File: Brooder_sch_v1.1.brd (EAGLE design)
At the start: 90 x 75 mm, 38 parts, among them J1 DCJ0202, J2 1X2-3.5MM, J3 DCJ0202, J4 1X2-3.5MM, T1 2N2222, U1 328P

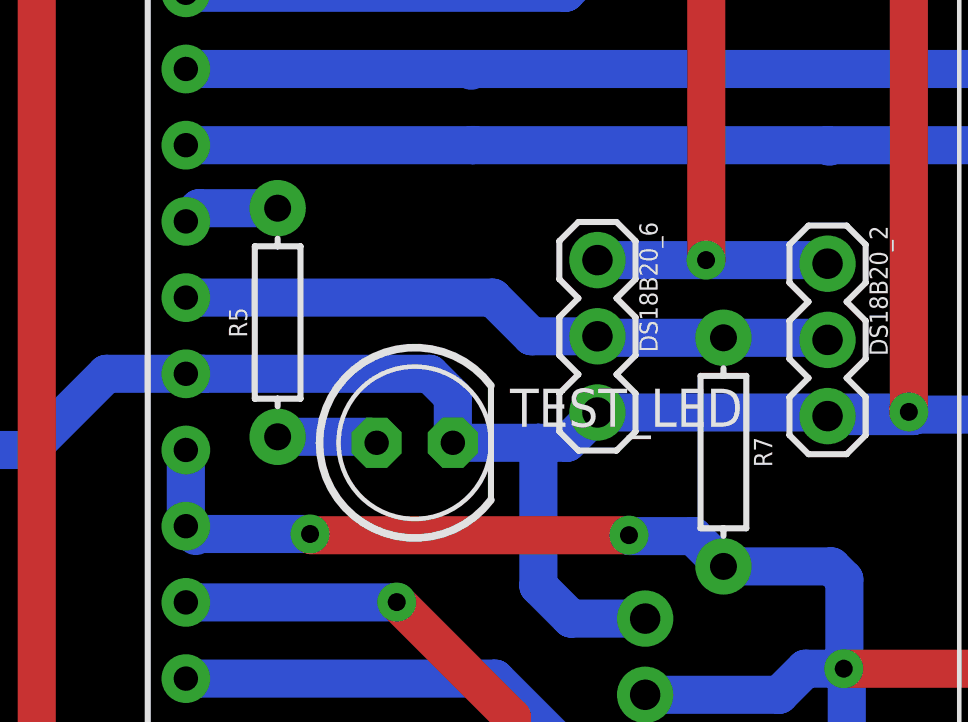
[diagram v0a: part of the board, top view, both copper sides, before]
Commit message: Removes test led fro  schematic
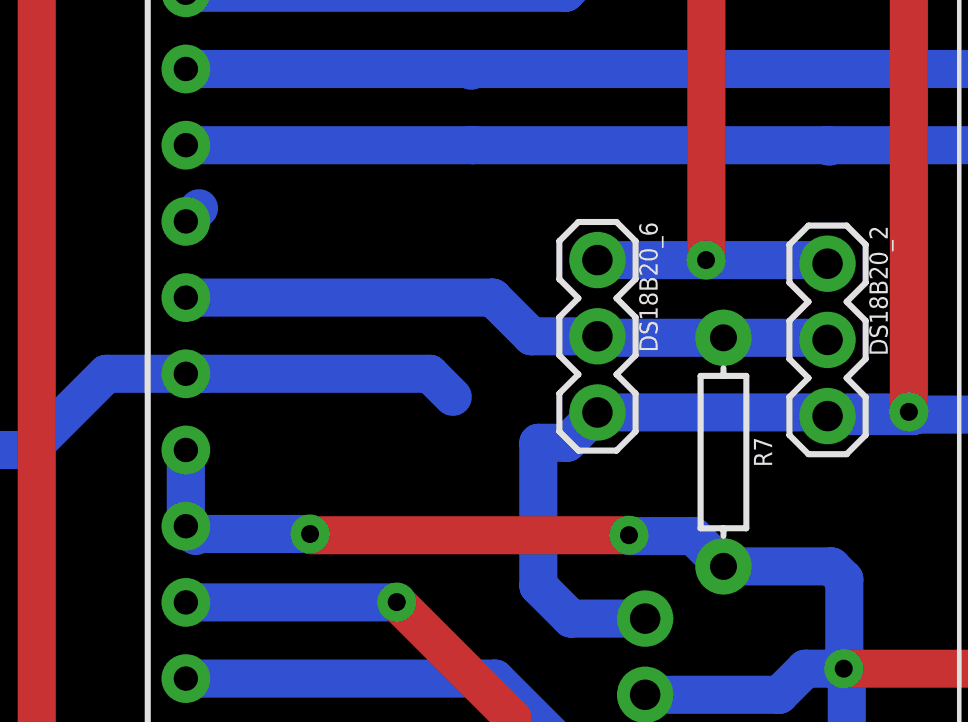
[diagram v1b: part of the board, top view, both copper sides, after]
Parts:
- removed R5: 220, SparkFun-Resistors:AXIAL-0.3
- removed TEST_LED: (no value), adafruit:LED5MM
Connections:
- removed net N$1: R5.P$1, TEST_LED.A
- net GND: no longer TEST_LED.K
- net PC1: no longer R5.P$2
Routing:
- net GND: track 386.0 -> 381.6 mm
- net N$1: track 3.38 -> 0.00 mm
- net PC1: track 3.24 -> 0.62 mm
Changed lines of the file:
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@@
 </element>
 <element name="J2" library="adafruit" package="1X2-3.5MM" value="1X2-3.5MM" x="69.84" y="69.63"/>
-<element name="R5" library="SparkFun-Resistors" package="AXIAL-0.3" value="220" x="45" y="43" rot="R90">
-<attribute name="PROD_ID" value="RES-09327" x="45" y="43" size="1.778" layer="27" rot="R90" display="off"/>
-</element>
-<element name="TEST_LED" library="adafruit" package="LED5MM" value="" x="49.57" y="38.99"/>
 <element name="DS3231" library="SparkFun-Connectors" package="1X06_NO_SILK" value="" x="49.13" y="61.27">
 <attribute name="PROD_ID" value="CONN-08437" x="49.13" y="61.27" size="1.778" layer="27" display="off"/>
@@
 <wire x1="20.24" y1="41.49" x2="19.72" y2="40.97" width="1.27" layer="16"/>
 <contactref element="FTDI" pad="2"/>
-<contactref element="TEST_LED" pad="K"/>
 <contactref element="DS3231" pad="6"/>
 <wire x1="4.31" y1="63.03" x2="14.31" y2="63.03" width="1.27" layer="1"/>
@@
 <wire x1="3.8" y1="24.42" x2="3.05" y2="24.42" width="1.27" layer="1"/>
 <wire x1="41.94" y1="41.29" x2="50.07" y2="41.29" width="1.27" layer="16"/>
-<wire x1="50.84" y1="40.52" x2="50.84" y2="38.99" width="1.27" layer="16"/>
 <wire x1="50.07" y1="41.29" x2="50.84" y2="40.52" width="1.27" layer="16"/>
-<wire x1="50.84" y1="38.99" x2="53.69" y2="38.99" width="1.27" layer="16"/>
 <wire x1="53.69" y1="38.99" x2="54.65" y2="38.99" width="1.27" layer="16"/>
 <wire x1="54.65" y1="38.99" x2="55.66" y2="40" width="1.27" layer="16"/>
@@
 <wire x1="5" y1="7" x2="4.19" y2="14.85" width="0" layer="19" extent="16-16"/>
 <wire x1="20.24" y1="41.49" x2="13.87" y2="52.87" width="0" layer="19" extent="1-16"/>
+<wire x1="53.69" y1="38.99" x2="50.84" y2="40.52" width="0" layer="19" extent="16-16"/>
 <wire x1="19.71" y1="34.8" x2="19.72" y2="39.62" width="0" layer="19" extent="1-1"/>
 <wire x1="1.4" y1="-82.36" x2="13" y2="2" width="0" layer="19" extent="16-16"/>
@@
 <wire x1="33.25" y1="5.25" x2="33.46" y2="5.46" width="1.27" layer="16"/>
 </signal>
-<signal name="N$1">
-<contactref element="R5" pad="P$1"/>
-<contactref element="TEST_LED" pad="A"/>
-<wire x1="45" y1="39.19" x2="48.1" y2="39.19" width="1.27" layer="16"/>
-<wire x1="48.1" y1="39.19" x2="48.3" y2="38.99" width="1.27" layer="16"/>
-</signal>
 <signal name="PC1">
 <contactref element="U1" pad="24"/>
-<contactref element="R5" pad="P$2"/>
 <wire x1="41.94" y1="46.37" x2="42.38" y2="46.81" width="1.27" layer="16"/>
-<wire x1="42.38" y1="46.81" x2="45" y2="46.81" width="1.27" layer="16"/>
 <contactref element="R6" pad="P$2"/>
 <wire x1="11.81" y1="-66.35" x2="41.94" y2="46.37" width="0" layer="19" extent="1-1"/>

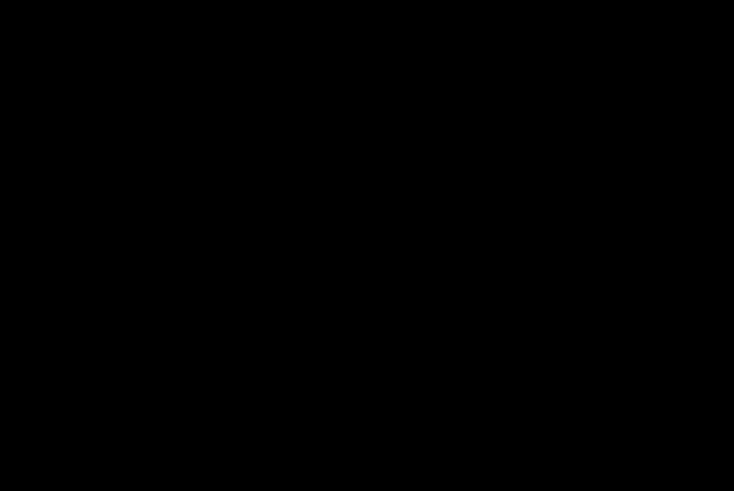
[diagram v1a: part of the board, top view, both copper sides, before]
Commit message: Adds extra terminal block to the relay
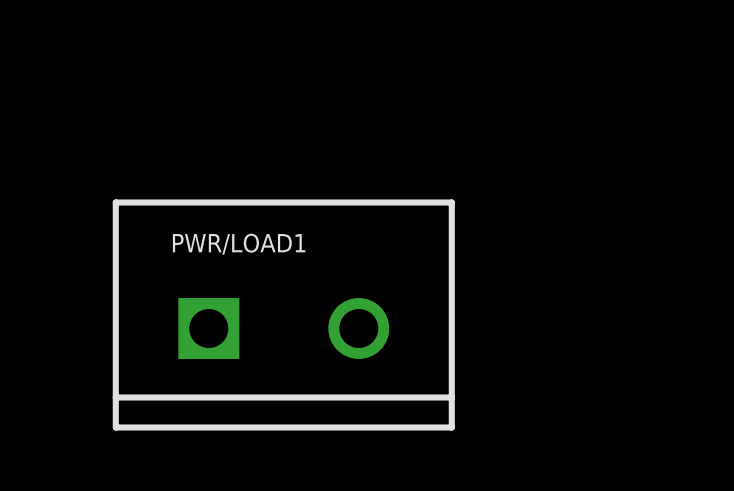
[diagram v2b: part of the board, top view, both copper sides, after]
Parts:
- added PWR/LOAD1: (no value), SparkFun-Connectors:SCREWTERMINAL-5MM-2
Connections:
- removed net N$14: PWR/LOAD.2, U$1.SWCOMMON
- new net N$1: PWR/LOAD1.2, U$1.SWCOMMON
- new net N$3: PWR/LOAD.2, PWR/LOAD1.1
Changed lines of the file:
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@@
 </element>
 <element name="LED2" library="adafruit" package="LED5MM" value="" x="30.86" y="-65.34"/>
+<element name="PWR/LOAD1" library="SparkFun-Connectors" package="SCREWTERMINAL-5MM-2" value="" x="4.96" y="-99.13">
+<attribute name="SF_SKU" value="PRT-08432" x="4.96" y="-99.13" size="1.778" layer="27" display="off"/>
+</element>
 </elements>
 <signals>
@@
 <wire x1="33.04" y1="-21.72" x2="15.84" y2="-30.6" width="0" layer="19" extent="1-1"/>
 </signal>
-<signal name="N$14">
+<signal name="N$1">
+<contactref element="PWR/LOAD1" pad="2"/>
 <contactref element="U$1" pad="SWCOMMON"/>
+<wire x1="1.84" y1="-24.6" x2="9.96" y2="-99.13" width="0" layer="19" extent="1-1"/>
+</signal>
+<signal name="N$3">
 <contactref element="PWR/LOAD" pad="2"/>
-<wire x1="38.04" y1="-21.72" x2="1.84" y2="-24.6" width="0" layer="19" extent="1-1"/>
+<contactref element="PWR/LOAD1" pad="1"/>
+<wire x1="38.04" y1="-21.72" x2="4.96" y2="-99.13" width="0" layer="19" extent="1-1"/>
 </signal>
 </signals>

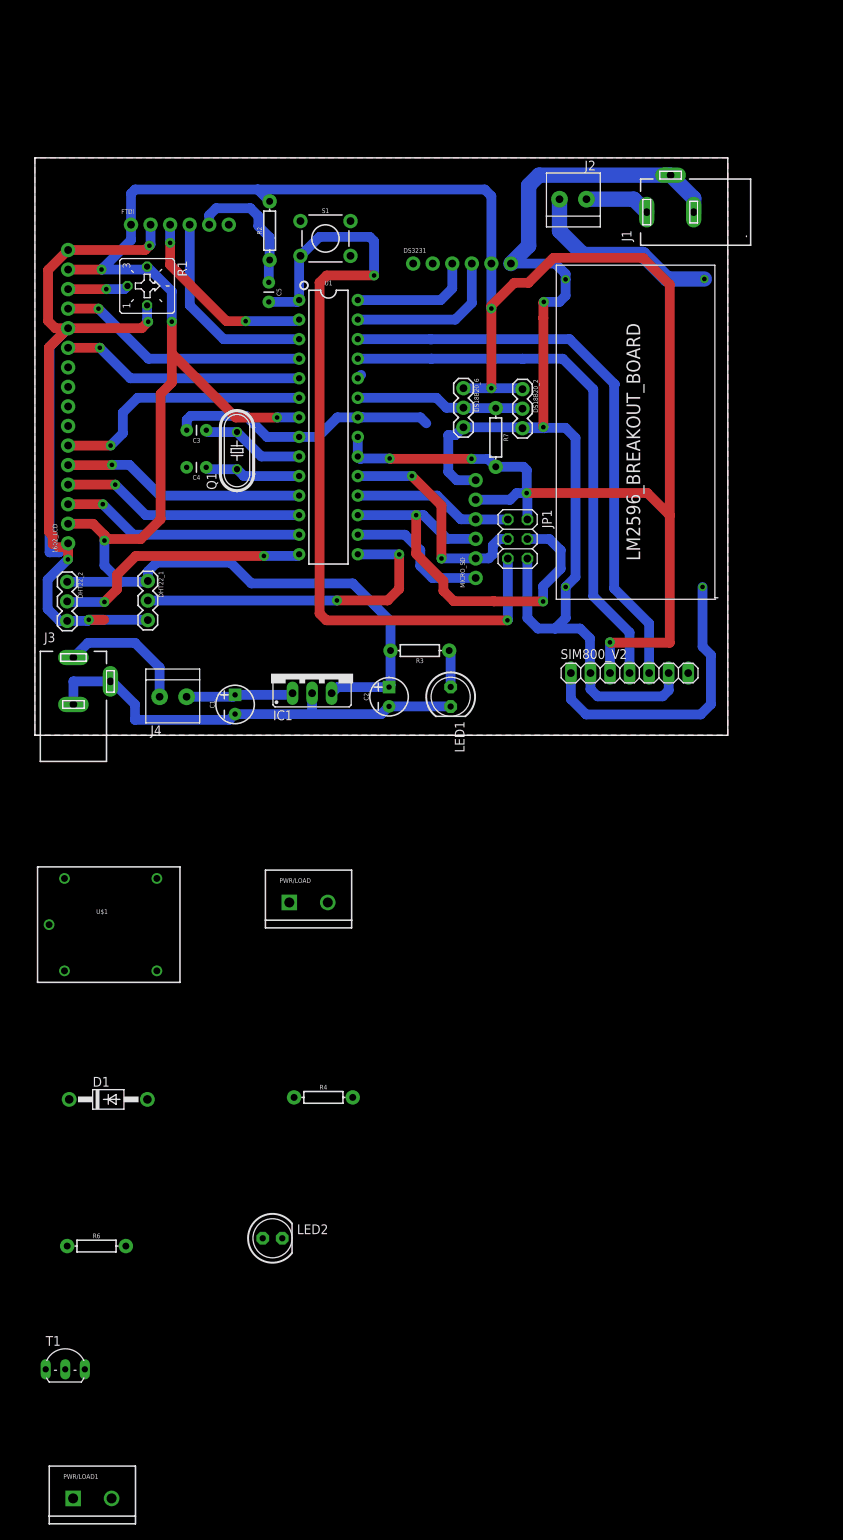
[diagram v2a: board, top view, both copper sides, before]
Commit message: Increases the size of the board from 90*75mm to 100*90mm
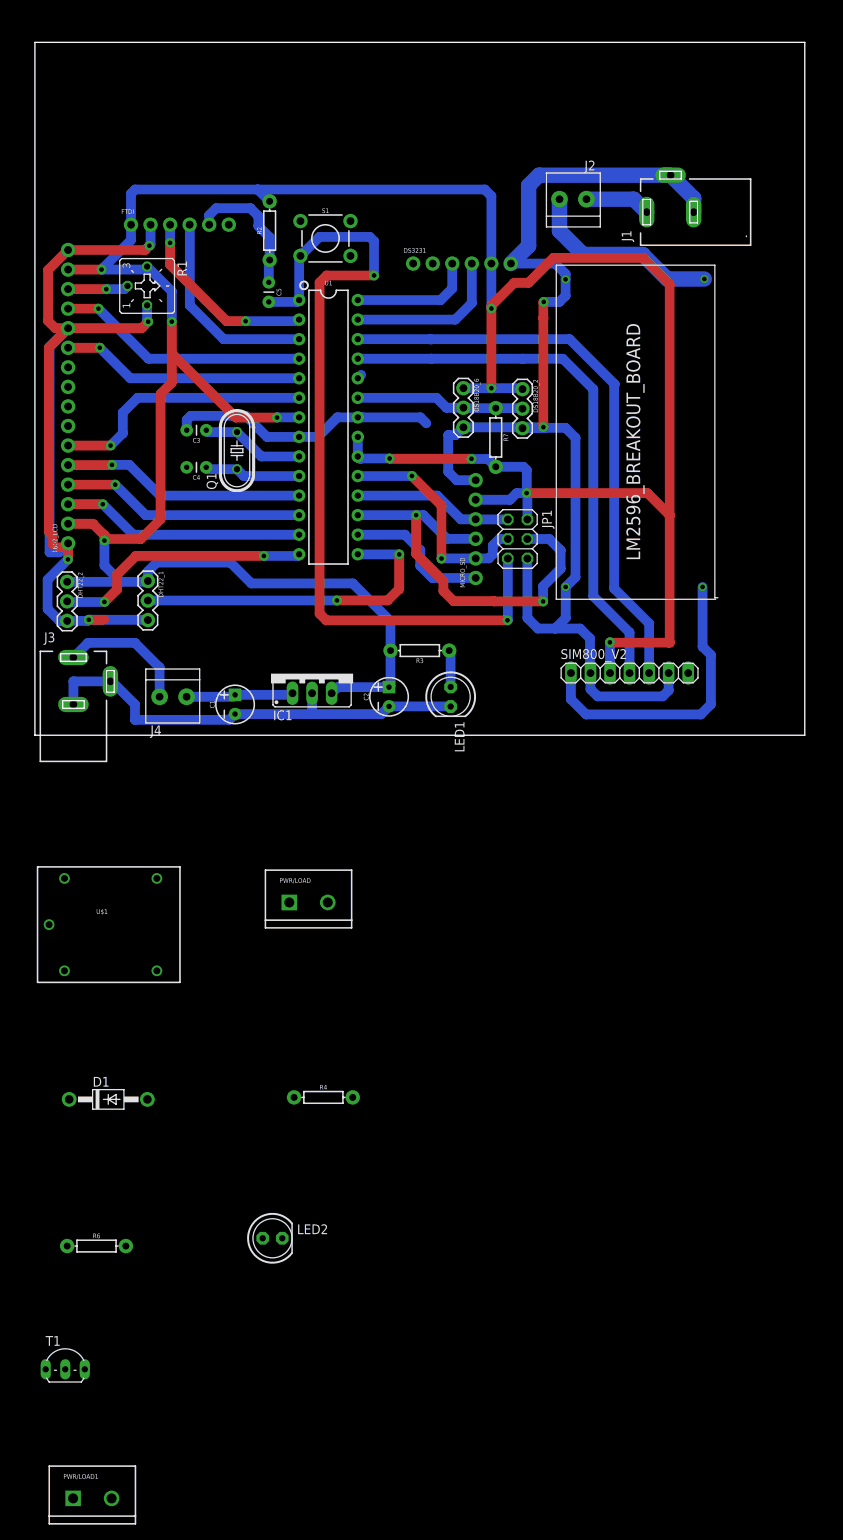
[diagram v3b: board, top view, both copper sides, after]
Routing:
- removed copper zone on layer 1, net GND
- removed copper zone on layer 16, net GND
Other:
- board size 90 x 75 mm -> 100 x 90 mm
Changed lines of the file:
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@@
 <setting verticaltext="up"/>
 </settings>
-<grid distance="0.01" unitdist="mm" unit="mm" style="lines" multiple="1" display="no" altdistance="5" altunitdist="mil" altunit="mil"/>
+<grid distance="1" unitdist="mm" unit="mm" style="lines" multiple="1" display="yes" altdistance="5" altunitdist="mil" altunit="mil"/>
 <layers>
 <layer number="1" name="Top" color="4" fill="1" visible="yes" active="yes"/>
@@
 <board>
 <plain>
-<wire x1="0" y1="0" x2="90" y2="0" width="0" layer="20"/>
-<wire x1="90" y1="0" x2="90" y2="75" width="0" layer="20"/>
-<wire x1="90" y1="75" x2="0" y2="75" width="0" layer="20"/>
-<wire x1="0" y1="75" x2="0" y2="0" width="0" layer="20"/>
-<dimension x1="75" y1="0" x2="75" y2="75" x3="99.12" y3="37.5" textsize="1.778" layer="20"/>
-<dimension x1="0" y1="0" x2="90" y2="0" x3="45" y3="-9.54" textsize="1.778" layer="20"/>
+<wire x1="0" y1="0" x2="100" y2="0" width="0" layer="20"/>
+<wire x1="100" y1="0" x2="100" y2="90" width="0" layer="20"/>
+<wire x1="100" y1="90" x2="0" y2="90" width="0" layer="20"/>
+<wire x1="0" y1="90" x2="0" y2="0" width="0" layer="20"/>
 </plain>
 <attributes>
@@
 <wire x1="66.1" y1="56.29" x2="68.13" y2="56.29" width="1.27" layer="16"/>
 <wire x1="68.13" y1="56.29" x2="68.9319125" y2="57.0919125" width="1.27" layer="16"/>
-<polygon width="1.27" layer="16" isolate="1.27">
-<vertex x="0" y="0"/>
-<vertex x="90" y="0"/>
-<vertex x="90" y="75"/>
-<vertex x="0" y="75"/>
-</polygon>
-<polygon width="1.27" layer="1" isolate="1.27">
-<vertex x="0" y="0"/>
-<vertex x="90" y="0"/>
-<vertex x="90" y="75"/>
-<vertex x="0" y="75"/>
-</polygon>
 <wire x1="26" y1="2.75" x2="35.75" y2="2.75" width="1.27" layer="16"/>
 <wire x1="35.75" y1="2.75" x2="36" y2="3" width="1.27" layer="16"/>

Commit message: Replaces ds3231 header pins with ds3231 symbol
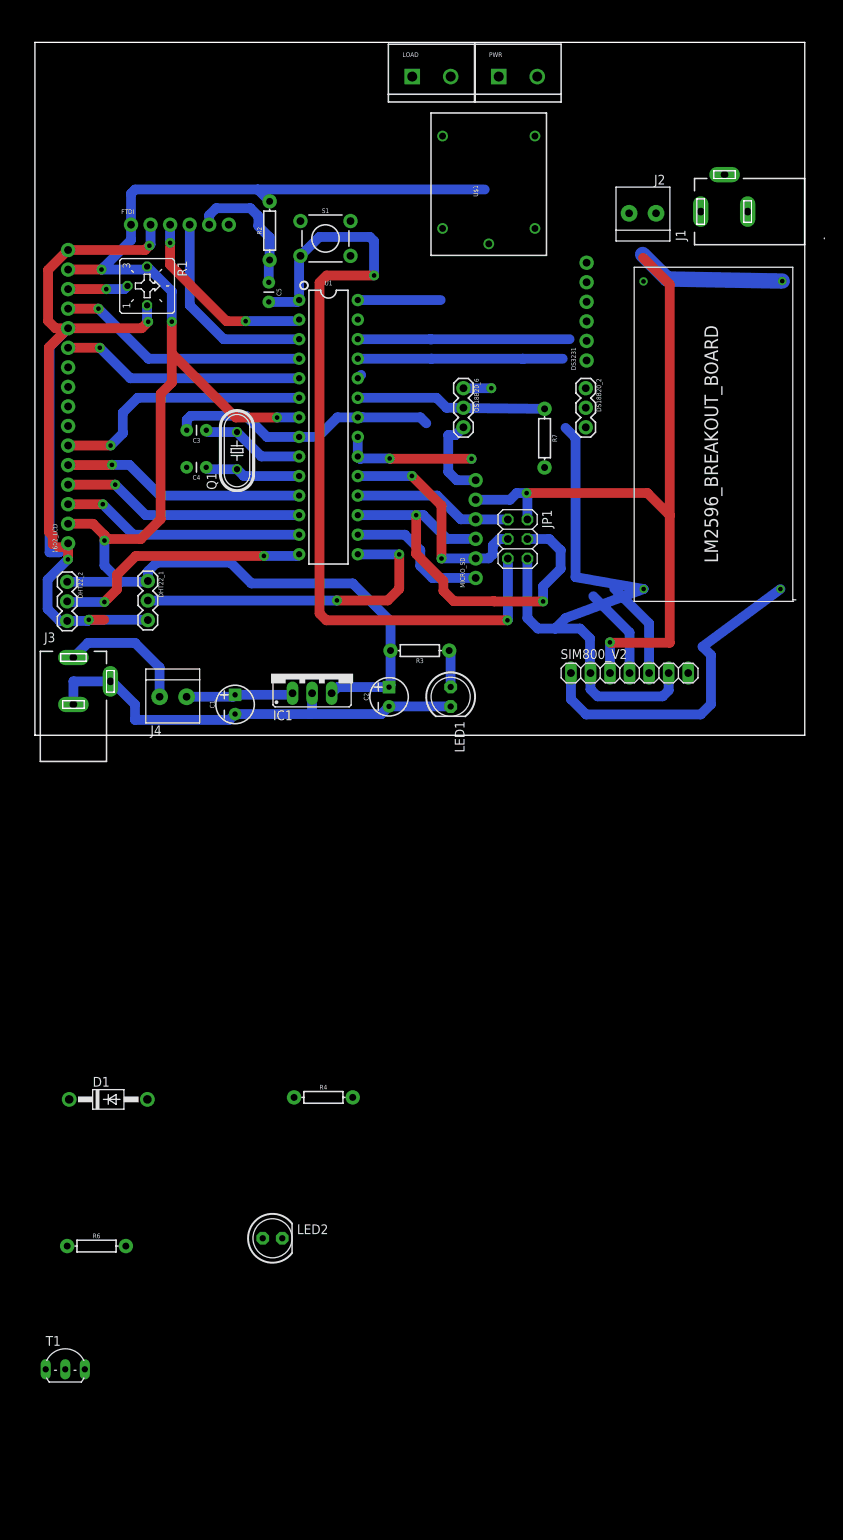
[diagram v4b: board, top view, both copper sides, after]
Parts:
- removed PWR/LOAD, PWR/LOAD1: (no value), SparkFun-Connectors:SCREWTERMINAL-5MM-2
- added LOAD, PWR: (no value), SparkFun-Connectors:SCREWTERMINAL-5MM-2
- moved U$1 107.8 mm to (58.8, 71.2), turned to 90 degrees
- moved DS3231 25.8 mm to (71.7, 48.7), turned to 90 degrees
- moved U$2 10.1 mm to (98.5, 17.5)
- moved J2 9.22 mm to (78.9, 67.8)
- moved DS18B20_2 8.22 mm to (71.5, 45.1)
- moved J1 7.01 mm to (89.6, 68.0)
- moved R7 6.34 mm to (66.2, 38.6)
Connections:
- net N$1: now also LOAD.2; no longer PWR/LOAD1.2
- net N$13: now also PWR.1; no longer PWR/LOAD.1
- net N$3: now also LOAD.1, PWR.2; no longer PWR/LOAD.2, PWR/LOAD1.1
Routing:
- net GND: track 381.6 -> 313.0 mm, vias 6 -> 4
- net 5V: track 388.9 -> 325.3 mm, vias 10 -> 9
- net RX: track 75.3 -> 40.5 mm
- net TX: track 71.1 -> 38.6 mm
- net PC4: track 20.8 -> 0.00 mm
- net 12V_SIM: track 8.53 -> 0.00 mm
- net 12V_S_SIM: track 25.5 -> 19.5 mm
- net PC5: track 16.1 -> 10.8 mm
- net 5V_SIM: track 38.6 -> 43.5 mm
- net PC0: track 22.0 -> 24.8 mm
